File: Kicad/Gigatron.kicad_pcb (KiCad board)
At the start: 2 copper layers, 234.9 x 158.8 mm, 154 parts, among them J1 54819-0519, J2 CONN-JACK-STEREO-R/A-3PIN-3.5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, J3 DB15_FEMALE_HighDensity_Mount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, J4 DB9_MALE_MountingHoles, U1 74HCT04, U10 74HCT244, U11 74HCT139, U12 74HCT153, U13 74HCT138, U14 74HCT138, U15 74HCT240, U16 74HCT32, U17 74HCT153, U18 74HCT153, U19 74HCT153, U2 MCP100-450DI, U20 74HCT153, U21 74HCT153, U22 74HCT153, U23 74HCT153, U24 74HCT153, U25 74HCT283, U26 74HCT283, U27 74HCT377, U28 74HCT244, U29 74HCT161, U3 74HCT161, U30 74HCT161, U31 74HCT377, U32 74HCT157, U33 74HCT157, U34 74HCT157, U35 74HCT157, U36 HM62256BLP-7, U37 74HCT377, U38 74HCT273, U39 74HC595, U4 74HCT161, U5 74HCT161, U6 74HCT161, U7 27C1024, U8 74HCT273, U9 74HCT273, Y1 6.25MHz/30pF

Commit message: Update to work with mostly the default KiCAD items or items downloaded via the KiCAD Libraries too.
2 Resistors added of 1k on the lines for TRUE and FALSE pull ups.

Several things deleted which appeared at Graphic shapes on the PCB sometimes
but could not be edited. this was done manually at the bottom of the PCB_KiCAD file.

Deleted some PCB items around the order which marked the Copper limits of top and bottom. may have been tied to TRUE & FALSE.

Changed USB socket type.

This has been done not to change the board but to aid understanding and allow anyone who wants slightly easier access.

I have not tested it and provide no warranty.

Signed-off-by: John Bradley <flypie@rocketmail.com>
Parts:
- removed ALU7, CLK1, CLK2, GND (x2): Measurement_Point_Square-TH_Small, Measurement_Points:Measurement_Point_Square-TH_Small
- removed REF** (x4): 1pin, Connectors:1pin
- added H1: MountingHole, MountingHole:MountingHole_2.7mm_M2.5, F.Cu at (23.5, 27.3)
- added H2: MountingHole, MountingHole:MountingHole_2.7mm_M2.5, F.Cu at (250.8, 27.3)
- added H3: MountingHole, MountingHole:MountingHole_2.7mm_M2.5, F.Cu at (23.5, 178.4)
- added H4: MountingHole, MountingHole:MountingHole_2.7mm_M2.5, F.Cu at (250.8, 178.4)
- added R100: 1K, Resistor_THT:R_Axial_DIN0204_L3.6mm_D1.6mm_P1.90mm_Vertical, F.Cu at (52.7, 44.5)
- added R101: 1K, Resistor_THT:R_Axial_DIN0204_L3.6mm_D1.6mm_P1.90mm_Vertical, F.Cu at (57.7, 44.5)
- A15: footprint Kicad:Breakout-1x1-MvK -> TestPoint:TestPoint_THTPad_D2.0mm_Drill1.0mm
- C1, C2, C3: footprint Capacitors_THT:C_Disc_D3.0mm_W2.0mm_P2.50mm -> Capacitor_THT:C_Disc_D3.0mm_W2.0mm_P2.50mm
- C10, C11, C12, C13, C14, C15, C16, C17, C18, C19, C20, C21, C22, C23, C24, C25, C26, C27, C28, C29, C30, C31, C32, C33, C34, C35, C36, C37, C38, C39, C40, C41, C42, C43, C44, C5, C6, C7, C8, C9: footprint Capacitors_THT:C_Disc_D4.3mm_W1.9mm_P5.00mm -> Capacitor_THT:C_Disc_D4.3mm_W1.9mm_P5.00mm
- C4: footprint Capacitors_THT:CP_Radial_D8.0mm_P3.50mm -> Capacitor_THT:CP_Radial_D8.0mm_P3.50mm
- D1: footprint Diodes_THT:D_DO-15_P12.70mm_Horizontal -> Diode_THT:D_DO-15_P12.70mm_Horizontal
- D10, D11, D12, D13, D14, D15, D16, D17, D18, D19, D20, D21, D22, D23, D24, D25, D26, D27, D28, D29, D30, D31, D32, D33, D34, D35, D36, D9: footprint Diodes_THT:D_A-405_P2.54mm_Vertical_KathodeUp -> Diode_THT:D_A-405_P2.54mm_Vertical_KathodeUp
- D2, D5, D6, D7, D8: footprint LEDs:LED_D3.0mm -> LED_THT:LED_D3.0mm
- D3, D4: footprint Diodes_THT:D_A-405_P7.62mm_Horizontal -> Diode_THT:D_A-405_P7.62mm_Horizontal
- F1: value 750mA/180mΩ/60V -> 750mA/180mohms/60V; footprint Fuse_Holders_and_Fuses:Fuse_TE5_Littlefuse-395Series -> Fuse:Fuse_Littelfuse_395Series
- J1: footprint 54819-0519-MvK:54819-0519-MvK -> Connector_USB:USB_Micro-B_Wuerth_629105150521
- J2: footprint Kicad:SJ1-3523N-MvK -> SamacSys_Parts_l:SJ13523N
- J3: footprint DB15:DB15_1734344_MvK -> Connector_Dsub:DSUB-15-HD_Female_Horizontal_P2.29x1.98mm_EdgePinOffset3.03mm_Housed_MountingHolesOffset4.94mm
- J4: footprint Connectors:DB9MD -> Connector_Dsub:DSUB-9_Female_Horizontal_P2.77x2.84mm_EdgePinOffset4.94mm_Housed_MountingHolesOffset7.48mm
- R1, R10, R11, R12, R13, R14, R15, R16, R17, R18, R19, R2, R3, R6, R7: footprint Resistors_THT:R_Axial_DIN0207_L6.3mm_D2.5mm_P10.16mm_Horizontal -> Resistor_THT:R_Axial_DIN0207_L6.3mm_D2.5mm_P10.16mm_Horizontal
- R4, R5, R8: footprint Resistors_THT:R_Array_SIP5 -> Resistor_THT:R_Array_SIP5
- R9: value R=10kΩ -> R=10kohms; footprint Resistors_THT:R_Array_SIP6 -> Resistor_THT:R_Array_SIP6
- U1, U16: footprint Kicad:DIP-14-MvK -> Package_DIP:DIP-14_W7.62mm
- U10, U15, U27, U28, U31, U37, U38, U8, U9: footprint Kicad:DIP-20-MvK -> Package_DIP:DIP-20_W7.62mm
- U11, U12, U13, U14, U17, U18, U19, U20, U21, U22, U23, U24, U25, U26, U29, U3, U30, U32, U33, U34, U35, U39, U4, U5, U6: footprint Kicad:DIP-16-MvK -> Package_DIP:DIP-16_W7.62mm
- U2: footprint TO_SOT_Packages_THT:TO-92_Inline_Wide -> Package_TO_SOT_THT:TO-92L_Inline_Wide
- U36: footprint Kicad:DIP-28-MvK -> Package_DIP:DIP-28_W15.24mm
- U7: footprint Kicad:DIP-40-MvK -> Package_DIP:DIP-40_W15.24mm
- Y1: footprint Crystals:Crystal_HC49-U_Vertical -> Crystal:Crystal_HC49-U_Vertical
- moved J2 6.35 mm to (86.4, 24.1)
- moved J4 6.35 mm to (226.1, 31.8)
- moved J1 5.72 mm to (33.0, 27.3), turned to 180 degrees
- moved J3 3.42 mm to (183.5, 31.1)
- moved F1 2.59 mm to (47.0, 35.6)
- moved Y1 2.48 mm to (187.6, 48.2)
- moved C5 0.90 mm to (204.5, 38.7)
- moved D2 0.63 mm to (173.4, 43.2)
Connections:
- C1 pad 2: L -> GND
- C10 pad 1: H -> VCC
- C10 pad 2: L -> GND
- C11 pad 1: H -> VCC
- C11 pad 2: L -> GND
- C12 pad 1: H -> VCC
- C12 pad 2: L -> GND
- C13 pad 1: H -> VCC
- C13 pad 2: L -> GND
- C14 pad 1: H -> VCC
- C14 pad 2: L -> GND
- C15 pad 1: H -> VCC
- C15 pad 2: L -> GND
- C16 pad 1: H -> VCC
- C16 pad 2: L -> GND
- C17 pad 1: H -> VCC
- C17 pad 2: L -> GND
- C18 pad 1: H -> VCC
- C18 pad 2: L -> GND
- C19 pad 1: H -> VCC
- C19 pad 2: L -> GND
- C2 pad 2: L -> GND
- C20 pad 1: H -> VCC
- C20 pad 2: L -> GND
- C21 pad 1: H -> VCC
- C21 pad 2: L -> GND
- C22 pad 1: H -> VCC
- C22 pad 2: L -> GND
- C23 pad 1: H -> VCC
- C23 pad 2: L -> GND
- C24 pad 1: H -> VCC
- C24 pad 2: L -> GND
- C25 pad 1: H -> VCC
- C25 pad 2: L -> GND
- C26 pad 1: H -> VCC
- C26 pad 2: L -> GND
- C27 pad 1: H -> VCC
- C27 pad 2: L -> GND
- C28 pad 1: H -> VCC
- C28 pad 2: L -> GND
- C29 pad 1: H -> VCC
- C29 pad 2: L -> GND
- C3 pad 2: L -> GND
- C30 pad 1: H -> VCC
- C30 pad 2: L -> GND
- C31 pad 1: H -> VCC
- C31 pad 2: L -> GND
- C32 pad 1: H -> VCC
- C32 pad 2: L -> GND
- C33 pad 1: H -> VCC
- C33 pad 2: L -> GND
- C34 pad 1: H -> VCC
- C34 pad 2: L -> GND
- C35 pad 1: H -> VCC
- C35 pad 2: L -> GND
- C36 pad 1: H -> VCC
- C36 pad 2: L -> GND
- C37 pad 1: H -> VCC
- C37 pad 2: L -> GND
- C38 pad 1: H -> VCC
- C38 pad 2: L -> GND
- C39 pad 1: H -> VCC
- C39 pad 2: L -> GND
- C4 pad 1: H -> VCC
- C4 pad 2: L -> GND
- C40 pad 1: H -> VCC
- C40 pad 2: L -> GND
- C41 pad 1: H -> VCC
- C41 pad 2: L -> GND
- C42 pad 1: H -> VCC
- C42 pad 2: L -> GND
- C43 pad 2: L -> GND
- C5 pad 1: H -> VCC
- C5 pad 2: L -> GND
- C6 pad 1: H -> VCC
- C6 pad 2: L -> GND
- C7 pad 1: H -> VCC
- C7 pad 2: L -> GND
- C8 pad 1: H -> VCC
- C8 pad 2: L -> GND
- C9 pad 1: H -> VCC
- C9 pad 2: L -> GND
- D1 pad 1: H -> VCC
- D1 pad 2: L -> GND
- F1 pad 1: H -> VCC
- J1 pad 2: Net-(J1-Pad2) -> (no net)
- J1 pad 3: Net-(J1-Pad3) -> (no net)
- J1 pad 4: Net-(J1-Pad4) -> GND
- J1 pad 5: L -> GND
- J2 pad 1: Net-(C44-Pad1) -> GND
- J2 pad 2: Net-(J2-Pad2) -> Net-(C44-Pad1)
- J2 pad 3: Net-(J2-Pad3) -> Net-(C44-Pad1)
- J3 pad 0: L -> GND
- J3 pad 10: L -> GND
- J3 pad 11: Net-(J3-Pad11) -> (no net)
- J3 pad 12: Net-(J3-Pad12) -> (no net)
- J3 pad 15: Net-(J3-Pad15) -> (no net)
- J3 pad 4: Net-(J3-Pad4) -> (no net)
- J3 pad 5: L -> GND
- J3 pad 6: L -> GND
- J3 pad 7: L -> GND
- J3 pad 8: L -> GND
- J3 pad 9: Net-(J3-Pad9) -> (no net)
- J4 pad 0: L -> GND
- J4 pad 1: Net-(J4-Pad1) -> (no net)
- J4 pad 5: Net-(J4-Pad5) -> (no net)
- J4 pad 6: H -> VCC
- J4 pad 7: Net-(J4-Pad7) -> (no net)
- J4 pad 8: L -> GND
- J4 pad 9: Net-(J4-Pad9) -> (no net)
- R10 pad 2: L -> GND
- R19 pad 1: H -> VCC
- R3 pad 2: L -> GND
- R4 pad 1: H -> VCC
- R5 pad 1: H -> VCC
- R6 pad 1: H -> VCC
- R7 pad 2: H -> VCC
- R8 pad 1: L -> GND
- R9 pad 6: L -> GND
- U1 pad 10: Net-(U1-Pad10) -> (no net)
- U1 pad 14: H -> VCC
- U1 pad 7: L -> GND
- U10 pad 10: L -> GND
- U10 pad 20: H -> VCC
- U11 pad 10: Net-(U11-Pad10) -> (no net)
- U11 pad 11: Net-(U11-Pad11) -> (no net)
- U11 pad 16: H -> GND
- U11 pad 8: L -> VCC
- U11 pad 9: Net-(U11-Pad9) -> (no net)
- U12 pad 16: H -> VCC
- U12 pad 8: L -> GND
- U12 pad 9: Net-(U12-Pad9) -> (no net)
- U13 pad 16: H -> VCC
- U13 pad 8: L -> GND
- U14 pad 16: H -> VCC
- U14 pad 8: L -> GND
- U15 pad 10: L -> GND
- U15 pad 20: H -> VCC
- U16 pad 14: H -> GND
- U16 pad 7: L -> VCC
- U17 pad 16: H -> VCC
- U17 pad 8: L -> GND
- U18 pad 16: H -> VCC
- U18 pad 8: L -> GND
- U19 pad 16: H -> VCC
- U19 pad 8: L -> GND
- U2 pad 2: H -> VCC
- U2 pad 3: L -> GND
- U20 pad 16: H -> VCC
- U20 pad 8: L -> GND
- U21 pad 16: H -> VCC
- U21 pad 8: L -> GND
- U22 pad 16: H -> VCC
- U22 pad 8: L -> GND
- U23 pad 16: H -> VCC
- U23 pad 8: L -> GND
- U24 pad 16: H -> VCC
- U24 pad 8: L -> GND
- U25 pad 16: H -> VCC
- U25 pad 8: L -> GND
- U26 pad 16: H -> VCC
- U26 pad 8: L -> GND
- U27 pad 10: L -> GND
- U27 pad 20: H -> VCC
- U28 pad 10: L -> GND
- U28 pad 20: H -> VCC
- U29 pad 16: H -> VCC
- U29 pad 8: L -> GND
- U3 pad 16: H -> VCC
- U3 pad 8: L -> GND
- U30 pad 15: Net-(U30-Pad15) -> (no net)
- U30 pad 16: H -> VCC
- U30 pad 8: L -> GND
- U31 pad 10: L -> GND
- U31 pad 20: H -> VCC
- U32 pad 16: H -> VCC
- U32 pad 8: L -> GND
- U33 pad 16: H -> VCC
- U33 pad 8: L -> GND
- U34 pad 16: H -> VCC
- U34 pad 8: L -> GND
- U35 pad 16: H -> VCC
- U35 pad 8: L -> GND
- U36 pad 14: L -> GND
- U36 pad 28: H -> VCC
- U37 pad 10: L -> GND
- U37 pad 20: H -> VCC
- U38 pad 10: L -> GND
- U38 pad 20: H -> VCC
- U39 pad 16: H -> VCC
- U39 pad 8: L -> GND
- U39 pad 9: Net-(U39-Pad9) -> (no net)
- U4 pad 16: H -> VCC
- U4 pad 8: L -> GND
- U5 pad 16: H -> VCC
- U5 pad 8: L -> GND
- U6 pad 15: Net-(U6-Pad15) -> (no net)
- U6 pad 16: H -> VCC
- U6 pad 8: L -> GND
- U7 pad 1: L -> GND
- U7 pad 11: L -> GND
- U7 pad 30: L -> GND
- U7 pad 38: Net-(U7-Pad38) -> (no net)
- U7 pad 40: H -> VCC
- U8 pad 10: L -> GND
- U8 pad 20: H -> VCC
- U9 pad 10: L -> GND
- U9 pad 20: H -> VCC
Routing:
- net L: track 4811.9 -> 747.2 mm, vias 278 -> 5
- net H: track 2536.5 -> 766.2 mm, vias 48 -> 5
- net GND: track 0.00 -> 1494.9 mm
- net VCC: track 0.00 -> 1098.2 mm
- net BUS5: track 588.0 -> 319.1 mm, vias 10 -> 8
- net BUS6: track 597.6 -> 329.1 mm, vias 11 -> 6
- net BUS7: track 634.9 -> 383.6 mm, vias 9 -> 8
- net BUS4: track 547.8 -> 320.7 mm, vias 11 -> 2
- net BUS1: track 570.4 -> 346.3 mm, vias 8 -> 4
- net BUS2: track 600.2 -> 389.5 mm, vias 8 -> 4
- net BUS3: track 638.8 -> 442.1 mm, vias 8 -> 2
- net BUS0: track 545.2 -> 351.3 mm, vias 6 -> 5
- net AL: track 405.8 -> 250.2 mm, vias 9 -> 3
- net AR0: track 410.7 -> 308.4 mm, vias 10 -> 4
- net AR1: track 353.5 -> 259.7 mm, vias 9 -> 1
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- removed copper zone on B.Cu, net L
- removed copper zone on F.Cu, net L
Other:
- outline, holes or cut-outs redrawn
- net class Power added: clearance 0.2, trace_width 0.4, via_dia 0.6, via_drill 0.4
- board text added: "Rev. 0000 JB"
- board text removed: "Rev. 2012 OSH"

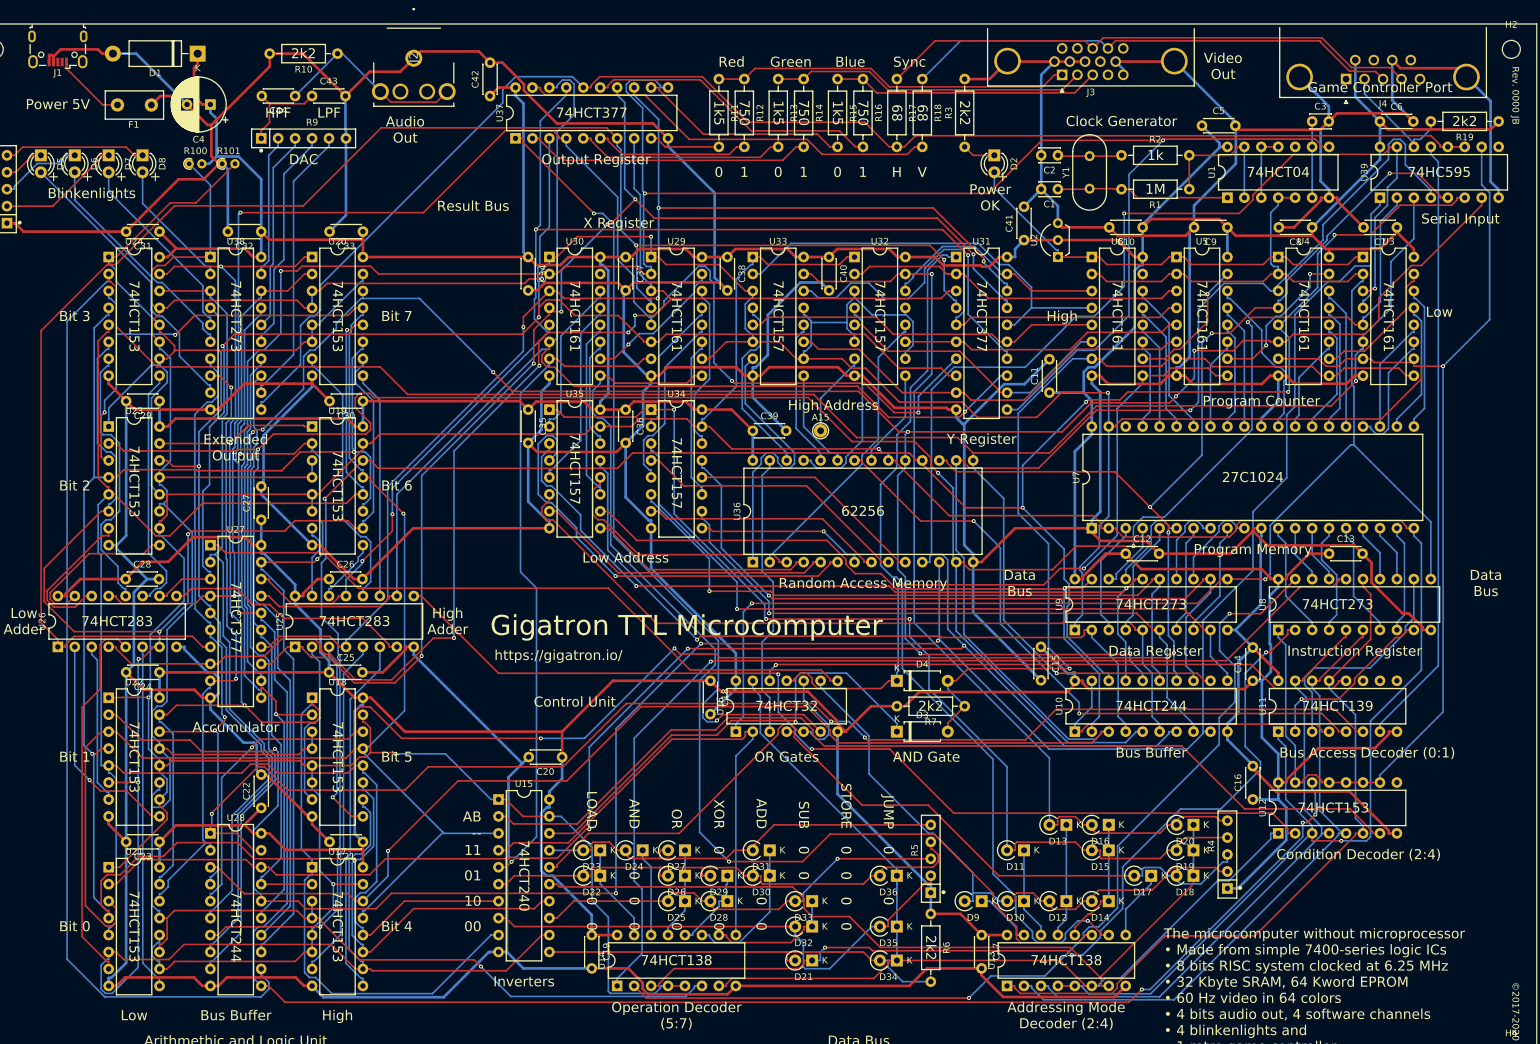
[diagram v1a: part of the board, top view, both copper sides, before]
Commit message: Run FreeRouting to completion. Update PCB and Gerbers.
Signed-off-by: John Bradley <flypie@rocketmail.com>
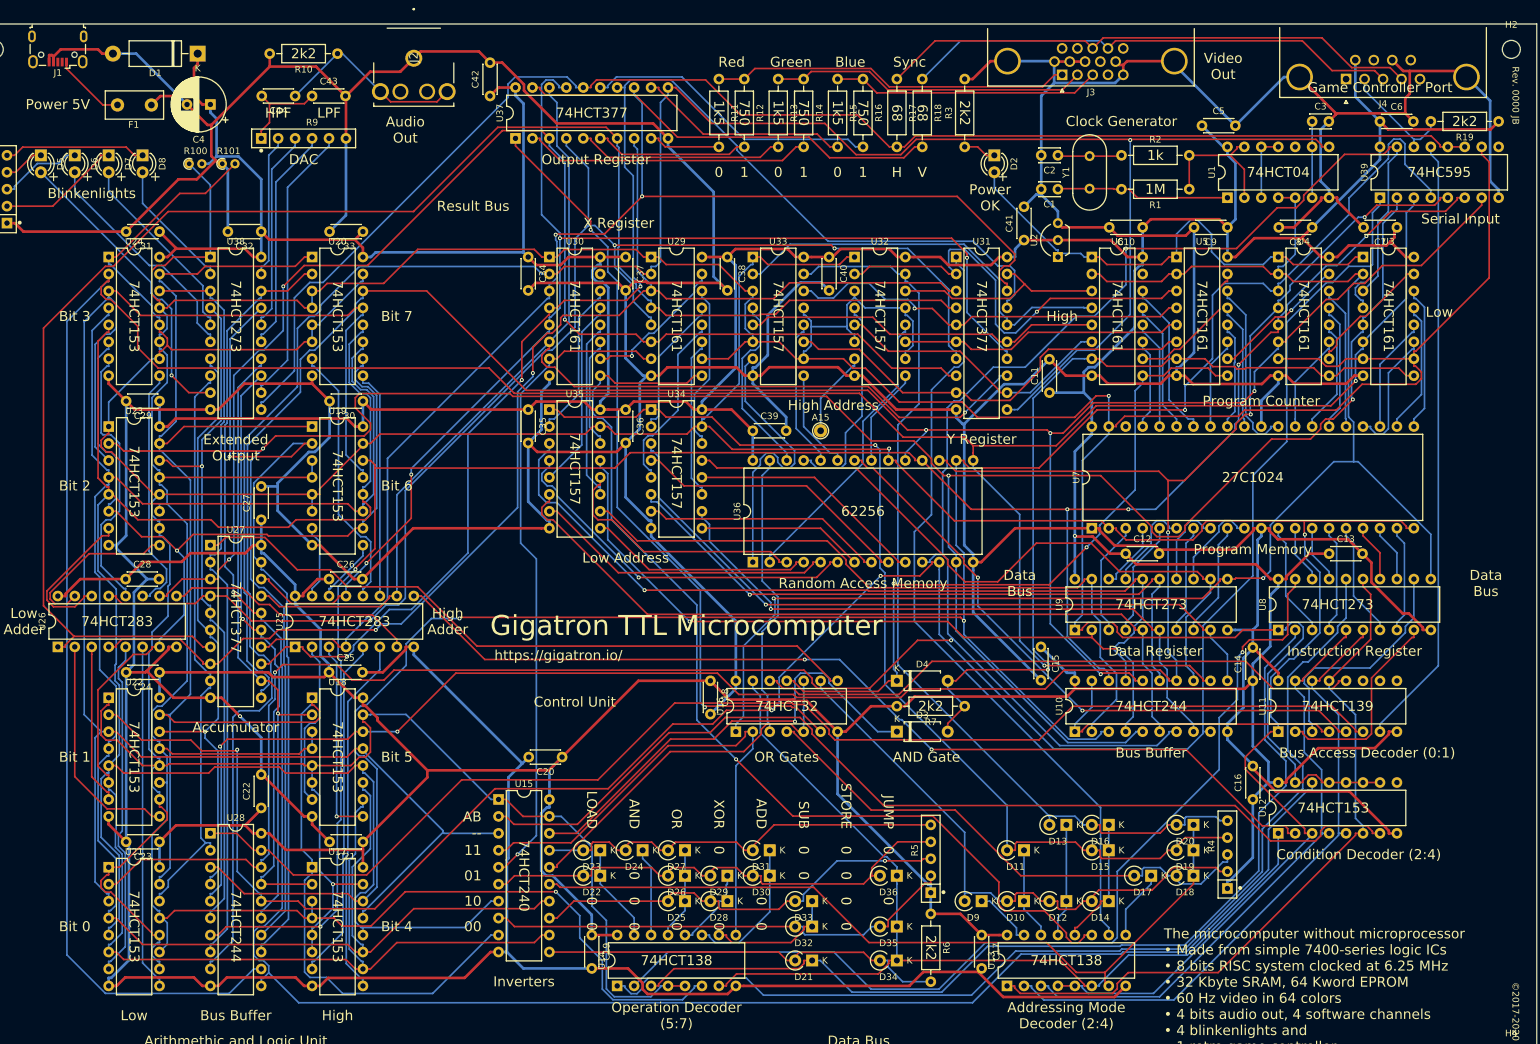
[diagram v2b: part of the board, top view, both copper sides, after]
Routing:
- net GND: track 1494.9 -> 1452.0 mm, vias 0 -> 1
- net AR0: track 308.4 -> 266.6 mm, vias 4 -> 1
- net H: track 766.2 -> 737.3 mm, vias 5 -> 2
- net ALU2: track 236.8 -> 214.1 mm, vias 4 -> 3
- net BUS7: track 383.6 -> 363.4 mm, vias 8 -> 4
- net L: track 747.2 -> 728.7 mm, vias 5 -> 3
- net CLK2: track 322.0 -> 304.7 mm, vias 3 -> 1
- net Y1: track 76.5 -> 61.1 mm, vias 0 -> 1
- net ~YL: track 132.6 -> 117.7 mm, vias 1 -> 0
- net Y0: track 51.2 -> 66.0 mm, vias 0 -> 1
- net ~XL: track 165.6 -> 151.2 mm
- net BUS6: track 329.1 -> 315.3 mm
- net BUS1: track 346.3 -> 333.4 mm, vias 4 -> 3
- net AR3: track 263.8 -> 276.3 mm, vias 3 -> 0
- net ALU0: track 204.0 -> 191.8 mm, vias 4 -> 2
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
